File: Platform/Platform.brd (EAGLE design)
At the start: 96.2 x 43.1 mm, 38 parts, among them U1 FT232RLSSOP, X1 USBSMD, Y1 RESONATORSMD

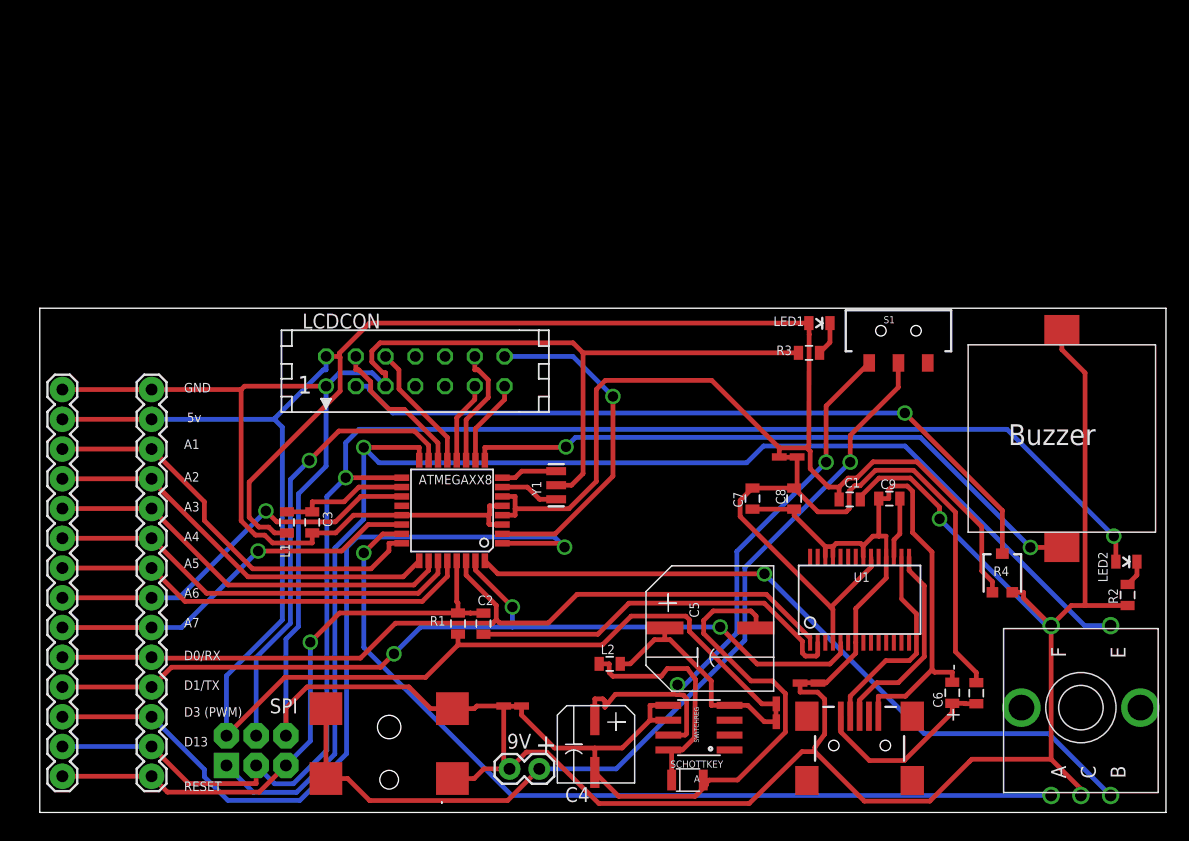
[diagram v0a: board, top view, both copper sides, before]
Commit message: Fixed typo and terminal spacing.
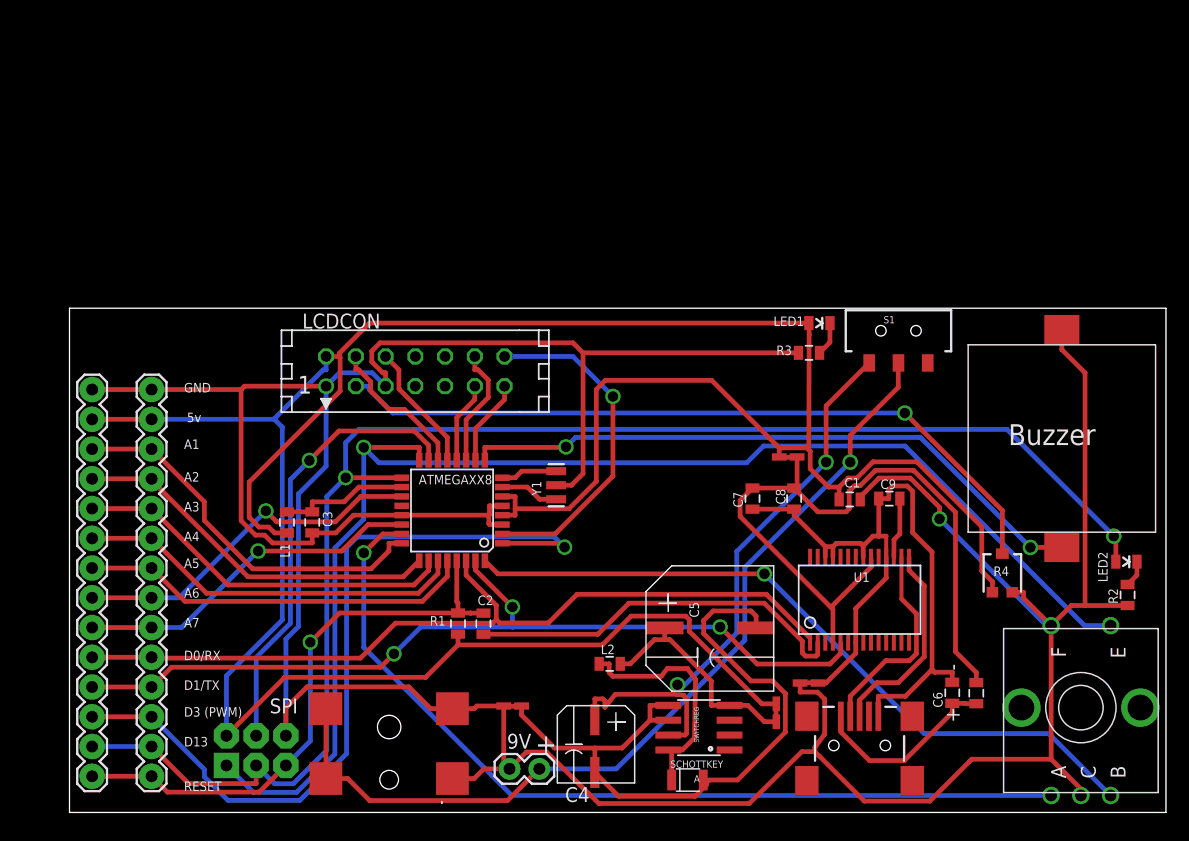
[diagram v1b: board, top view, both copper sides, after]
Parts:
- moved JP1 2.54 mm to (5.08, 36.0)
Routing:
- net GND: track 321.8 -> 319.2 mm
- net VCC: track 253.0 -> 250.4 mm
- net RX: track 74.4 -> 71.9 mm
- net D13/SCK: track 131.1 -> 128.5 mm
- net RESET: track 52.3 -> 49.8 mm
- net D3: track 71.6 -> 69.1 mm
- net A5: track 36.3 -> 33.7 mm
- net A1: track 35.4 -> 32.9 mm
- net A7: track 32.6 -> 30.1 mm
- net A6: track 33.3 -> 30.8 mm
- net A3: track 35.3 -> 32.8 mm
- net A2: track 34.6 -> 32.1 mm
- net TX: track 78.2 -> 75.6 mm
- net A4: track 35.8 -> 33.3 mm
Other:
- board size 96.2 x 43.1 mm -> 93.6 x 43.1 mm
- board text added: "Robotic Minion Starter Kit"
- board text removed: "Robotit Minion Starter Kit"
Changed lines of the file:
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@@
 <setting verticaltext="up"/>
 </settings>
-<grid distance="1" unitdist="mil" unit="inch" style="lines" multiple="1" display="yes" altdistance="0.1" altunitdist="mil" altunit="mil"/>
+<grid distance="0.1" unitdist="inch" unit="inch" style="lines" multiple="1" display="yes" altdistance="0.1" altunitdist="mil" altunit="mil"/>
 <layers>
 <layer number="1" name="Top" color="11" fill="9" visible="yes" active="yes"/>
@@
 <board>
 <plain>
-<wire x1="0.6096" y1="-0.127" x2="96.774" y2="-0.127" width="0" layer="20"/>
+<wire x1="3.1496" y1="-0.127" x2="96.774" y2="-0.127" width="0" layer="20"/>
 <wire x1="96.774" y1="-0.127" x2="96.774" y2="42.926" width="0" layer="20"/>
-<wire x1="96.774" y1="42.926" x2="0.6096" y2="42.926" width="0" layer="20"/>
-<wire x1="0.6096" y1="42.926" x2="0.6096" y2="-0.127" width="0" layer="20"/>
+<wire x1="96.774" y1="42.926" x2="3.1496" y2="42.926" width="0" layer="20"/>
+<wire x1="3.1496" y1="42.926" x2="3.1496" y2="-0.127" width="0" layer="20"/>
 <rectangle x1="29.21" y1="19.304" x2="44.45" y2="33.02" layer="43"/>
 <text x="42.926" y="4.826" size="1.778" layer="25">+</text>
@@
 <text x="59.2074" y="26.8732" size="0.8128" layer="26" ratio="10" rot="MR0">http://on.fb.me/JXJ9oD</text>
 <text x="68.9102" y="32.893" size="0.8128" layer="26" ratio="15" rot="MR0">http://creativecommons.org/licenses/by/2.0/</text>
-<text x="60.198" y="19.304" size="1.778" layer="26" rot="MR0">Robotit Minion Starter Kit</text>
+<text x="60.198" y="19.304" size="1.778" layer="26" rot="MR0">Robotic Minion Starter Kit</text>
 <text x="69.2404" y="9.271" size="1.778" layer="26" rot="MR0">By Dustin Andrews and David Andrews</text>
 <text x="8.56488125" y="35.557459375" size="0.8128" layer="26" ratio="10" rot="MR0">GND</text>
@@
 <element name="FTDIVCCLINK" library="Dustin" package="ISOLATOR" value="LINK" x="64.516" y="30.226" rot="R180"/>
 <element name="FTDIDGNDLINK" library="Dustin" package="ISOLATOR" value="LINK" x="66.294" y="10.922"/>
-<element name="JP1" library="Dustin" package="1X14B" value="M14B" x="2.54" y="35.9814" smashed="yes" rot="R270"/>
+<element name="JP1" library="Dustin" package="1X14B" value="M14B" x="5.08" y="35.9814" smashed="yes" rot="R270"/>
 <element name="C7" library="SparkFun" package="0805" value="0.1uf" x="61.468" y="26.67" smashed="yes" rot="R90">
 <attribute name="NAME" x="60.6425" y="25.908" size="0.8128" layer="25" ratio="10" rot="R90"/>
@@
 <wire x1="51.1085" y1="16.6374" x2="48.6459" y2="14.1748" width="0.4064" layer="1"/>
 <wire x1="48.6459" y1="14.1748" x2="36.322" y2="14.1748" width="0.4064" layer="1"/>
-<wire x1="2.54" y1="33.4414" x2="10.16" y2="33.4414" width="0.4064" layer="1"/>
+<wire x1="5.08" y1="33.4414" x2="10.16" y2="33.4414" width="0.4064" layer="1"/>
 <wire x1="10.16" y1="33.4414" x2="20.6506" y2="33.4414" width="0.4064" layer="16"/>
 <wire x1="25.0577" y1="38.8078" x2="26.1891" y2="38.8078" width="0.4064" layer="1"/>
@@
 <wire x1="72.2771" y1="28.4267" x2="70.6678" y2="26.8174" width="0.4064" layer="1"/>
 <wire x1="70.6678" y1="26.8174" x2="70.6678" y2="26.5954" width="0.4064" layer="1"/>
-<wire x1="10.16" y1="35.9814" x2="2.54" y2="35.9814" width="0.4064" layer="1"/>
+<wire x1="10.16" y1="35.9814" x2="5.08" y2="35.9814" width="0.4064" layer="1"/>
 <wire x1="40.2267" y1="8.9594" x2="40.2267" y2="3.5916" width="0.4064" layer="1"/>
 <wire x1="40.723" y1="3.5916" x2="40.2267" y2="3.5916" width="0.4064" layer="1"/>
@@
 <wire x1="27.8756" y1="32.5859" x2="83.1966" y2="32.5859" width="0.4064" layer="16"/>
 <wire x1="83.1966" y1="32.5859" x2="92.3197" y2="23.4628" width="0.4064" layer="16"/>
-<wire x1="2.54" y1="5.5014" x2="10.16" y2="5.5014" width="0.4064" layer="16"/>
+<wire x1="5.08" y1="5.5014" x2="10.16" y2="5.5014" width="0.4064" layer="16"/>
 <wire x1="92.4958" y1="21.2852" x2="92.4958" y2="23.3282" width="0.4064" layer="1"/>
 <wire x1="92.4958" y1="23.3282" x2="92.3544" y2="23.4696" width="0.4064" layer="1"/>
@@
 <contactref element="JP2" pad="3"/>
 <contactref element="JP1" pad="3"/>
-<wire x1="2.54" y1="30.9014" x2="10.16" y2="30.9014" width="0.4064" layer="1"/>
+<wire x1="5.08" y1="30.9014" x2="10.16" y2="30.9014" width="0.4064" layer="1"/>
 <wire x1="10.16" y1="30.9014" x2="14.6658" y2="26.3956" width="0.4064" layer="1"/>
 <wire x1="14.6658" y1="26.3956" x2="14.6658" y2="24.7954" width="0.4064" layer="1"/>
@@
 <contactref element="JP2" pad="4"/>
 <contactref element="JP1" pad="4"/>
-<wire x1="2.54" y1="28.3614" x2="10.16" y2="28.3614" width="0.4064" layer="1"/>
+<wire x1="5.08" y1="28.3614" x2="10.16" y2="28.3614" width="0.4064" layer="1"/>
 <wire x1="10.16" y1="28.3614" x2="10.16" y2="28.2244" width="0.4064" layer="1"/>
 <wire x1="10.16" y1="28.2244" x2="18.3956" y2="19.9888" width="0.4064" layer="1"/>
@@
 <contactref element="JP2" pad="5"/>
 <contactref element="JP1" pad="5"/>
-<wire x1="2.54" y1="25.8214" x2="10.16" y2="25.8214" width="0.4064" layer="1"/>
+<wire x1="5.08" y1="25.8214" x2="10.16" y2="25.8214" width="0.4064" layer="1"/>
 <wire x1="10.16" y1="25.8214" x2="16.6887" y2="19.2927" width="0.4064" layer="1"/>
 <wire x1="16.6887" y1="19.2927" x2="32.5522" y2="19.2927" width="0.4064" layer="1"/>
@@
 <contactref element="JP2" pad="6"/>
 <contactref element="JP1" pad="6"/>
-<wire x1="2.54" y1="23.2814" x2="10.16" y2="23.2814" width="0.4064" layer="1"/>
+<wire x1="5.08" y1="23.2814" x2="10.16" y2="23.2814" width="0.4064" layer="1"/>
 <wire x1="34.614" y1="21.3614" x2="34.614" y2="20.2691" width="0.4064" layer="1"/>
 <wire x1="34.614" y1="20.2691" x2="32.9306" y2="18.5857" width="0.4064" layer="1"/>
@@
 <contactref element="JP2" pad="7"/>
 <contactref element="JP1" pad="7"/>
-<wire x1="2.54" y1="20.7414" x2="10.16" y2="20.7414" width="0.4064" layer="1"/>
+<wire x1="5.08" y1="20.7414" x2="10.16" y2="20.7414" width="0.4064" layer="1"/>
 <wire x1="10.16" y1="20.7414" x2="13.0076" y2="17.8938" width="0.4064" layer="1"/>
 <wire x1="13.0076" y1="17.8938" x2="33.2733" y2="17.8938" width="0.4064" layer="1"/>
@@
 <wire x1="66.3766" y1="14.7721" x2="66.3766" y2="14.3884" width="0.3478" layer="1"/>
 <wire x1="66.3766" y1="14.3884" x2="66.387" y2="14.378" width="0.3478" layer="1"/>
-<wire x1="2.54" y1="13.1214" x2="10.16" y2="13.1214" width="0.4064" layer="1"/>
+<wire x1="5.08" y1="13.1214" x2="10.16" y2="13.1214" width="0.4064" layer="1"/>
 <wire x1="39.5919" y1="16.3373" x2="39.5919" y2="17.5569" width="0.4064" layer="1"/>
 <wire x1="39.5919" y1="17.5569" x2="37.014" y2="20.1348" width="0.4064" layer="1"/>
@@
 <via x="30.8545" y="13.4171" extent="1-16" drill="0.889" diameter="1.3336"/>
 <via x="40.9663" y="17.4167" extent="1-16" drill="0.889" diameter="1.3336"/>
-<wire x1="10.16" y1="10.5814" x2="2.54" y2="10.5814" width="0.4064" layer="1"/>
+<wire x1="10.16" y1="10.5814" x2="5.08" y2="10.5814" width="0.4064" layer="1"/>
 <wire x1="69.0056" y1="14.1126" x2="69.0056" y2="14.3594" width="0.3478" layer="1"/>
 <wire x1="69.0056" y1="14.3594" x2="68.987" y2="14.378" width="0.3478" layer="1"/>
@@
 <contactref element="JP1" pad="12"/>
 <via x="45.423" y="22.5242" extent="1-16" drill="0.889" diameter="1.3336"/>
-<wire x1="10.16" y1="8.0414" x2="2.54" y2="8.0414" width="0.4064" layer="1"/>
+<wire x1="10.16" y1="8.0414" x2="5.08" y2="8.0414" width="0.4064" layer="1"/>
 <wire x1="40.1066" y1="22.854" x2="45.0932" y2="22.854" width="0.4064" layer="1"/>
 <wire x1="45.0932" y1="22.854" x2="45.423" y2="22.5242" width="0.4064" layer="1"/>
@@
 <wire x1="11.5153" y1="1.6061" x2="19.3476" y2="1.6061" width="0.4064" layer="1"/>
 <wire x1="19.3476" y1="1.6061" x2="21.6276" y2="3.8861" width="0.4064" layer="1"/>
-<wire x1="2.54" y1="2.9614" x2="10.16" y2="2.9614" width="0.4064" layer="1"/>
+<wire x1="5.08" y1="2.9614" x2="10.16" y2="2.9614" width="0.4064" layer="1"/>
 <wire x1="21.6276" y1="3.8861" x2="23.7131" y2="5.9716" width="0.4064" layer="16"/>
 <wire x1="23.7131" y1="5.9716" x2="23.7131" y2="14.4083" width="0.4064" layer="16"/>
@@
 <contactref element="JP1" pad="8"/>
 <via x="19.919" y="25.6164" extent="1-16" drill="0.889" diameter="1.3336"/>
-<wire x1="2.54" y1="18.2014" x2="10.16" y2="18.2014" width="0.4064" layer="1"/>
+<wire x1="5.08" y1="18.2014" x2="10.16" y2="18.2014" width="0.4064" layer="1"/>
 <wire x1="10.16" y1="18.2014" x2="12.504" y2="18.2014" width="0.4064" layer="16"/>
 <wire x1="12.504" y1="18.2014" x2="19.919" y2="25.6164" width="0.4064" layer="16"/>
@@
 <contactref element="JP1" pad="9"/>
 <via x="19.2535" y="22.1933" extent="1-16" drill="0.889" diameter="1.3336"/>
-<wire x1="10.16" y1="15.6614" x2="2.54" y2="15.6614" width="0.4064" layer="1"/>
+<wire x1="10.16" y1="15.6614" x2="5.08" y2="15.6614" width="0.4064" layer="1"/>
 <wire x1="10.16" y1="15.6614" x2="12.7216" y2="15.6614" width="0.4064" layer="16"/>
 <wire x1="12.7216" y1="15.6614" x2="19.2535" y2="22.1933" width="0.4064" layer="16"/>
@@
 </signal>
 </signals>
-<errors>
-</errors>
 </board>
 </drawing>

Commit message: switched back to LDO
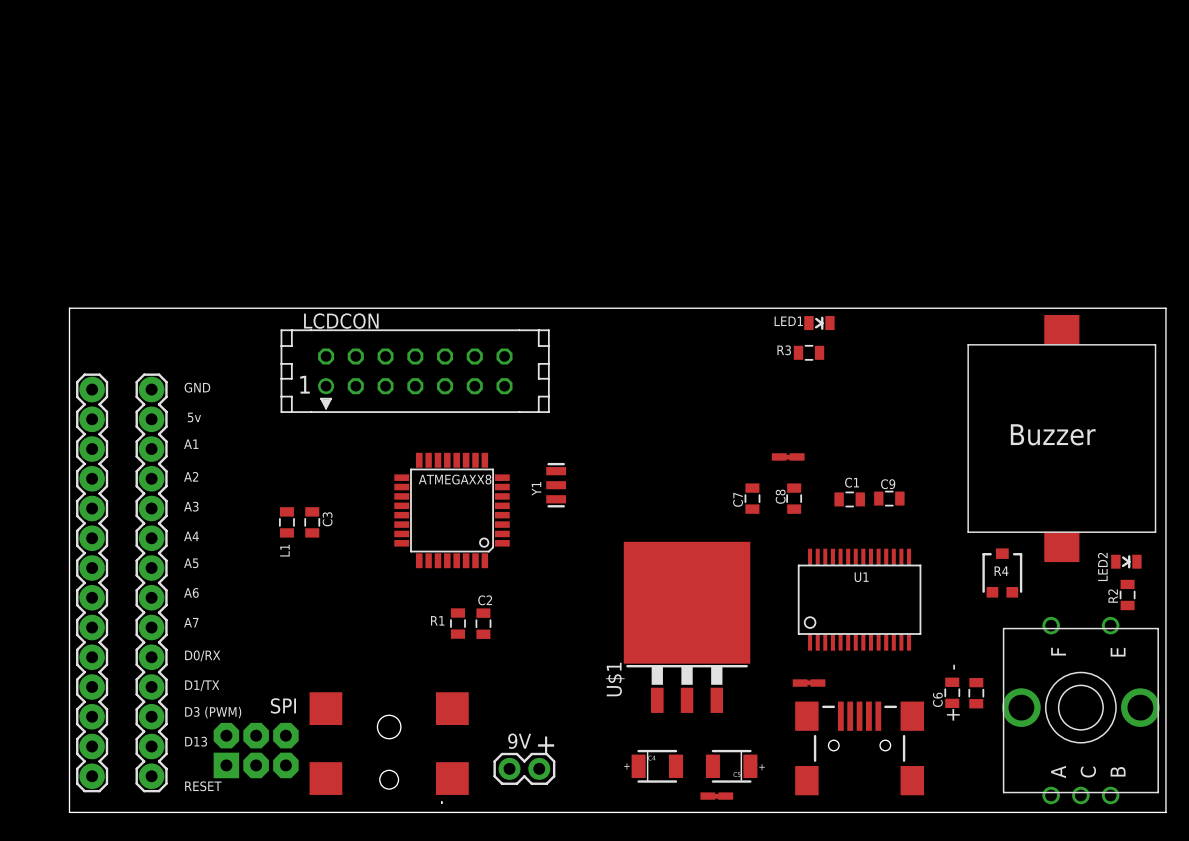
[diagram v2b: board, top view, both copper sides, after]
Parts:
- removed L2: 100uH, SparkFun:0805
- removed LINK1, LINK2: LINK, Dustin:ISOLATOR
- removed S1: (no value), Dustin:SWITCH-SPDT-SMT
- removed SCHOTTKEY: (no value), Dustin:SOD-123
- removed SWITCHREG: LM2594, Dustin:SOIC8
- added LDO_VCC_LINK: LINK, Dustin:ISOLATOR
- added U$1: IFX25001TC, Dustin:TO263-3
- C4: value 68uf -> 22UF 16V 478-1682-1-ND; device Dustin:F80 -> Dustin:1210POL
- C5: value 120uf -> 22UF 16V 478-1682-1-ND; device Dustin:10X8CAP -> Dustin:1210POL
- moved C5 11.5 mm to (59.7, 3.81), turned to 180 degrees
- moved C4 5.62 mm to (53.3, 3.81)
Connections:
- removed net GNDLINK: C4.-, C5.-, LINK2.P$1, SCHOTTKEY.ANODE, SWITCHREG.5, SWITCHREG.6
- removed net N$3: L2.1, SCHOTTKEY.CATHODE, SWITCHREG.8
- removed net RAW: C4.+, S1.1, SWITCHREG.7
- removed net VCCLINK: C5.+, L2.2, LINK1.P$1, SWITCHREG.4
- new net LDO_OUT: C5.1, LDO_VCC_LINK.P$1, U$1.3
- net GND: now also C4.2, C5.2, U$1.2, U$1.TAB; no longer LINK2.P$2
- net RAW_IN: now also C4.1, U$1.1; no longer S1.2
- net VCC: now also LDO_VCC_LINK.P$2; no longer LINK1.P$2
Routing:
- net GND: track 319.2 -> 0.00 mm, vias 1 -> 0
- net VCC: track 250.4 -> 0.00 mm
- net D13/SCK: track 128.5 -> 0.00 mm, vias 2 -> 0
- net D12/MISO: track 115.9 -> 0.00 mm, vias 1 -> 0
- net RAW_IN: track 77.3 -> 0.00 mm, vias 1 -> 0
- net A0: track 75.9 -> 0.00 mm, vias 1 -> 0
- net TX: track 75.6 -> 0.00 mm, vias 3 -> 0
- net RX: track 71.9 -> 0.00 mm
- net D3: track 69.1 -> 0.00 mm, vias 1 -> 0
- net FTDI-GND: track 64.7 -> 0.00 mm
- net CONTRAST: track 63.5 -> 0.00 mm, vias 1 -> 0
- net FTDI-VCC: track 62.7 -> 0.00 mm
- net D2: track 61.7 -> 0.00 mm, vias 1 -> 0
- net GNDLINK: track 59.7 -> 0.00 mm
- net D5: track 54.6 -> 0.00 mm, vias 2 -> 0
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
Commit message: wiring traces added
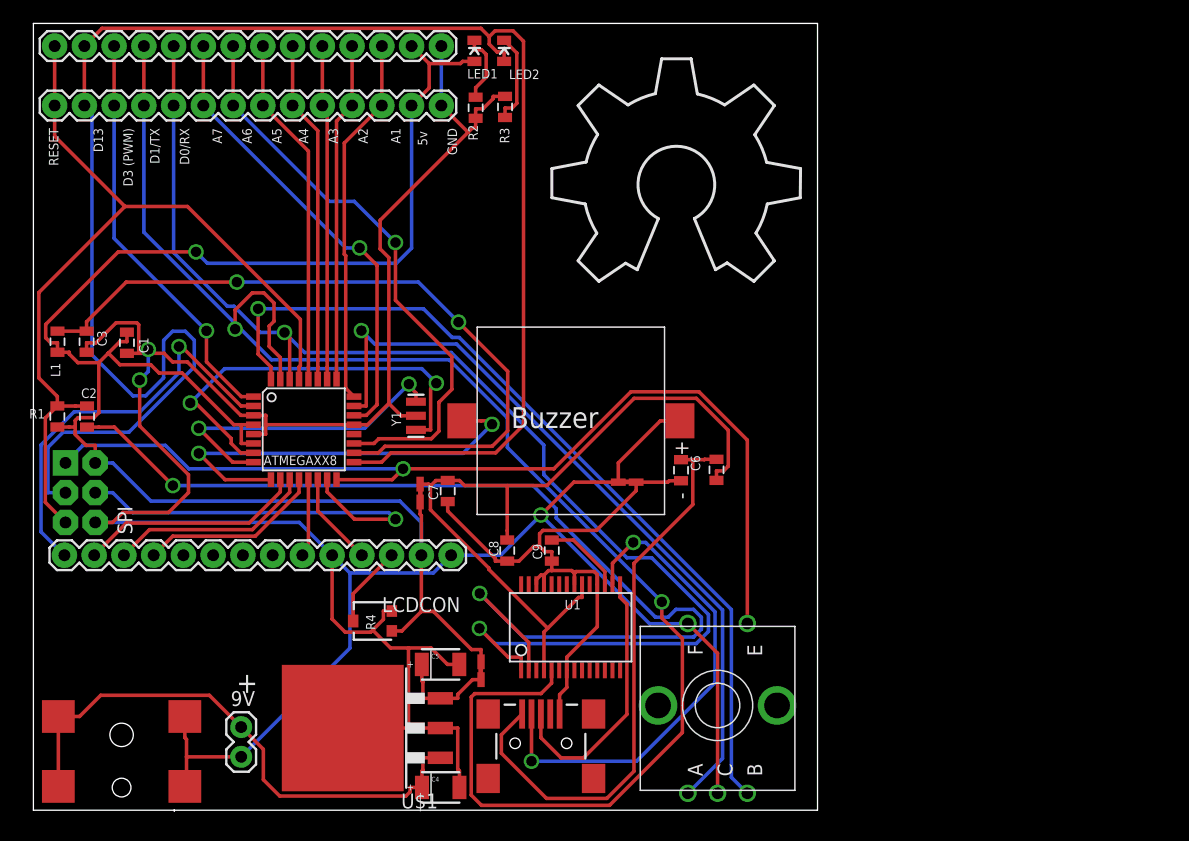
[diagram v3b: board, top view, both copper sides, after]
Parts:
- LCDCON: value (none) -> M14B; device con-harting:CON14 -> Dustin:1X14B
- moved R2 69.5 mm to (37.8, 60.0)
- moved LED2 68.7 mm to (40.3, 64.9), turned to 90 degrees
- moved C1 63.1 mm to (8.05, 40.0), turned to 90 degrees
- moved LOGO1 55.9 mm to (44.3, 45.2), flipped to the top
- moved R4 53.9 mm to (29.0, 16.2), turned to 90 degrees
- moved SG2 42.0 mm to (46.0, 33.3), turned to 180 degrees
- moved JP1 41.8 mm to (34.9, 65.3), turned to 180 degrees
- moved R1 38.5 mm to (2.11, 33.7)
- moved C2 38.2 mm to (4.65, 33.7)
- moved LED1 37.5 mm to (37.7, 64.9), turned to 90 degrees
- moved JP2 34.6 mm to (34.9, 60.2), turned to 180 degrees
- moved R3 33.4 mm to (40.3, 60.1), turned to 270 degrees
- moved FTDIVCCLINK 31.6 mm to (33.1, 27.1), turned to 270 degrees
- moved U$1 31.3 mm to (26.5, 7.08), turned to 90 degrees
- moved U$2 31.0 mm to (58.5, 1.51)
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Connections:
- net N$2: now also R3.2; no longer R2.2
- net N$7: now also R2.2; no longer R3.2
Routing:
- net GND: track 0.00 -> 266.1 mm, vias 0 -> 3
- net D13/SCK: track 0.00 -> 154.8 mm
- net VCC: track 0.00 -> 151.5 mm, vias 0 -> 1
- net TX: track 0.00 -> 137.7 mm, vias 0 -> 2
- net RX: track 0.00 -> 109.4 mm, vias 0 -> 2
- net DTR: track 0.00 -> 90.3 mm, vias 0 -> 2
- net D12/MISO: track 0.00 -> 85.8 mm, vias 0 -> 1
- net RESET: track 0.00 -> 74.7 mm
- net D2: track 0.00 -> 73.8 mm, vias 0 -> 1
- net FTDI-VCC: track 0.00 -> 65.8 mm
- net A0: track 0.00 -> 65.2 mm, vias 0 -> 1
- net AVCC: track 0.00 -> 62.8 mm, vias 0 -> 2
- net FTDI-GND: track 0.00 -> 50.6 mm
- net A6: track 0.00 -> 50.0 mm, vias 0 -> 1
- net VBUS: track 0.00 -> 49.7 mm
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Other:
- board size 93.6 x 43.1 mm -> 67 x 67.2 mm
- board text added: "D0"
- board text added: "D1"
- board text added: "D3"
- board text added: "RST"
- board text removed: "D3-PWM"
